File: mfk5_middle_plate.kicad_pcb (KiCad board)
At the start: 2 copper layers, 57.2 x 57.2 mm, 9 parts

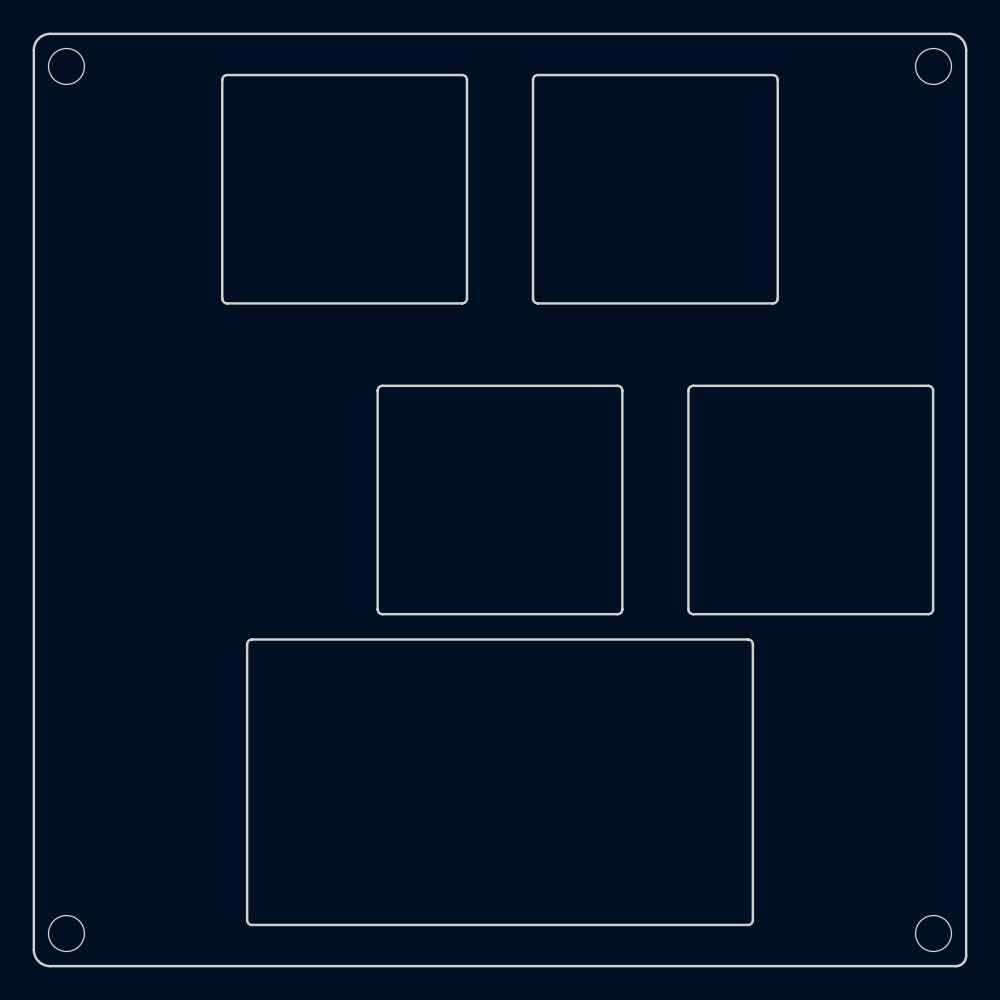
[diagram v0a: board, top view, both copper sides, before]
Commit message: Add ATmega32u4 and related components.
Stop using Pro Micro, going to use PCBA to SMT components.
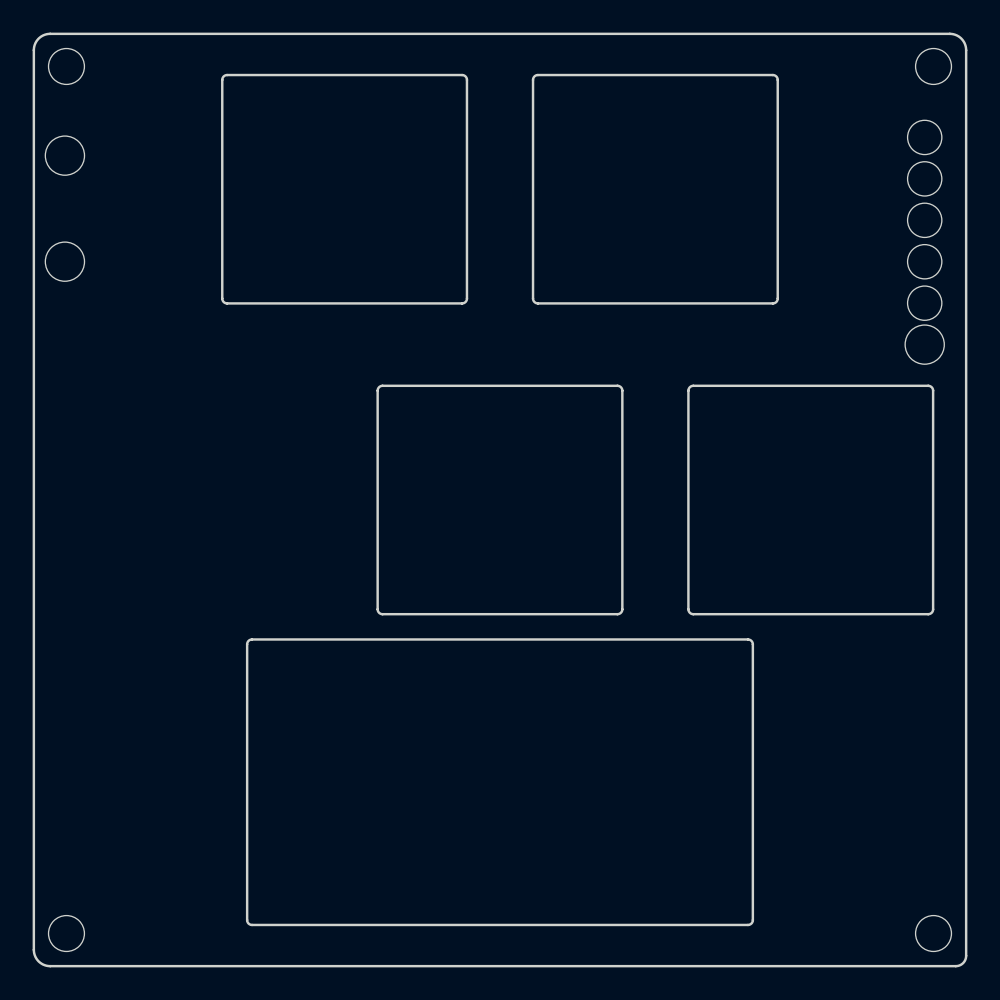
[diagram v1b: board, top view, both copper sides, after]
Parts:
- added REF**: , , F.Cu at (174.5, 95.0)
- added REF**: , , F.Cu at (174.5, 92.5)
- added REF**: , , F.Cu at (121.8, 90.0)
- added REF**: , , F.Cu at (122.5, 116.9)
- added REF**: , , F.Cu at (126.6, 125.6)
- added REF**: , , F.Cu at (170.8, 118.9)
- added REF**: , , F.Cu at (122.5, 125.6)
- added REF**: , , F.Cu at (174.5, 90.0)
- added REF**: , , F.Cu at (174.5, 87.4)
- added REF**: , , F.Cu at (166.8, 118.9)
- added REF**: , , F.Cu at (121.8, 83.5)
- added REF**: , , F.Cu at (165.6, 123.7)
- added REF**: , , F.Cu at (174.5, 82.3)
- added REF**: , , F.Cu at (173.8, 118.9)
- added REF**: , , F.Cu at (174.5, 84.9)
- added REF**: , , F.Cu at (126.6, 116.9)
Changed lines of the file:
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@@
   (title_block
     (title "mfk5 Middle Plate")
-    (date "2023-11-23")
-    (rev "2")
+    (date "2023-12-15")
+    (rev "3")
     (company "@niw")
   )
@@
   )
   (net 0 "")
+  (footprint "" (layer "F.Cu")
+    (at 174.46 95.05)
+    (fp_text reference "REF**" (at 0 0) (layer "F.SilkS") hide
+        (effects (font (size 1.27 1.27) (thickness 0.15)))
+    )
+    (fp_text value "" (at 0 0) (layer "F.SilkS") hide
+        (effects (font (size 1.27 1.27) (thickness 0.15)))
+    )
+    (pad "" np_thru_hole circle (at 0 0) (size 2.4 2.4) (drill 2.4) (layers "F&B.Cu" "*.Mask")
+      (pinfunction "Pin_1") (pintype "passive"))
+  )
+  (footprint "" (layer "F.Cu")
+    (at 121.755 83.465625)
+    (fp_text reference "REF**" (at 0 0) (layer "F.SilkS") hide
+        (effects (font (size 1.27 1.27) (thickness 0.15)))
+    )
+    (fp_text value "" (at 0 0) (layer "F.SilkS") hide
+        (effects (font (size 1.27 1.27) (thickness 0.15)))
+    )
+    (pad "" np_thru_hole circle (at 0 0 270) (size 2.4 2.4) (drill 2.4) (layers "F&B.Cu" "*.Mask")
+      (pinfunction "1") (pintype "passive"))
+  )
   (footprint "Gateron_Low_Profile:Gateron_Low_Profile_Middle_Plate" (layer "F.Cu")
     (at 157.95 85.525)
@@
     (pad "" np_thru_hole circle (at 0 0) (size 2.2 2.2) (drill 2.2) (layers "F&B.Cu" "*.Mask"))
   )
+  (footprint "" (layer "F.Cu")
+    (at 174.46 84.89)
+    (fp_text reference "REF**" (at 0 0) (layer "F.SilkS") hide
+        (effects (font (size 1.27 1.27) (thickness 0.15)))
+    )
+    (fp_text value "" (at 0 0) (layer "F.SilkS") hide
+        (effects (font (size 1.27 1.27) (thickness 0.15)))
+    )
+    (pad "" np_thru_hole circle (at 0 0) (size 2.1 2.1) (drill 2.1) (layers "F&B.Cu" "*.Mask")
+      (pinfunction "Pin_5") (pintype "passive"))
+  )
+  (footprint "" (layer "F.Cu")
+    (at 126.63 116.92375)
+    (fp_text reference "REF**" (at 0 0) (layer "F.SilkS") hide
+        (effects (font (size 1.27 1.27) (thickness 0.15)))
+    )
+    (fp_text value "" (at 0 0) (layer "F.SilkS") hide
+        (effects (font (size 1.27 1.27) (thickness 0.15)))
+    )
+    (pad "" np_thru_hole oval (at 0 0 90) (size 1.4 2.5) (drill oval 1.4 2.5) (layers "F&B.Cu" "*.Mask")
+      (pinfunction "SHIELD") (pintype "passive"))
+  )
+  (footprint "" (layer "F.Cu")
+    (at 174.46 92.51)
+    (fp_text reference "REF**" (at 0 0) (layer "F.SilkS") hide
+        (effects (font (size 1.27 1.27) (thickness 0.15)))
+    )
+    (fp_text value "" (at 0 0) (layer "F.SilkS") hide
+        (effects (font (size 1.27 1.27) (thickness 0.15)))
+    )
+    (pad "" np_thru_hole circle (at 0 0) (size 2.1 2.1) (drill 2.1) (layers "F&B.Cu" "*.Mask")
+      (pinfunction "Pin_2") (pintype "passive"))
+  )
+  (footprint "" (layer "F.Cu")
+    (at 121.755 89.965625)
+    (fp_text reference "REF**" (at 0 0) (layer "F.SilkS") hide
+        (effects (font (size 1.27 1.27) (thickness 0.15)))
+    )
+    (fp_text value "" (at 0 0) (layer "F.SilkS") hide
+        (effects (font (size 1.27 1.27) (thickness 0.15)))
+    )
+    (pad "" np_thru_hole circle (at 0 0 270) (size 2.4 2.4) (drill 2.4) (layers "F&B.Cu" "*.Mask")
+      (pinfunction "2") (pintype "passive"))
+  )
+  (footprint "" (layer "F.Cu")
+    (at 122.45 116.92375)
+    (fp_text reference "REF**" (at 0 0) (layer "F.SilkS") hide
+        (effects (font (size 1.27 1.27) (thickness 0.15)))
+    )
+    (fp_text value "" (at 0 0) (layer "F.SilkS") hide
+        (effects (font (size 1.27 1.27) (thickness 0.15)))
+    )
+    (pad "" np_thru_hole oval (at 0 0 90) (size 1.4 2) (drill oval 1.4 2) (layers "F&B.Cu" "*.Mask")
+      (pinfunction "SHIELD") (pintype "passive"))
+  )
+  (footprint "" (layer "F.Cu")
+    (at 126.63 125.56375)
+    (fp_text reference "REF**" (at 0 0) (layer "F.SilkS") hide
+        (effects (font (size 1.27 1.27) (thickness 0.15)))
+    )
+    (fp_text value "" (at 0 0) (layer "F.SilkS") hide
+        (effects (font (size 1.27 1.27) (thickness 0.15)))
+    )
+    (pad "" np_thru_hole oval (at 0 0 90) (size 1.4 2.5) (drill oval 1.4 2.5) (layers "F&B.Cu" "*.Mask")
+      (pinfunction "SHIELD") (pintype "passive"))
+  )
+  (footprint "" (layer "F.Cu")
+    (at 170.775 118.8625)
+    (fp_text reference "REF**" (at 0 0) (layer "F.SilkS") hide
+        (effects (font (size 1.27 1.27) (thickness 0.15)))
+    )
+    (fp_text value "" (at 0 0) (layer "F.SilkS") hide
+        (effects (font (size 1.27 1.27) (thickness 0.15)))
+    )
+    (pad "" np_thru_hole oval (at 0 0 90) (size 2 2.4) (drill oval 2 2.4) (layers "F&B.Cu" "*.Mask")
+      (pinfunction "Ring_1") (pintype "passive"))
+  )
+  (footprint "" (layer "F.Cu")
+    (at 122.45 125.56375)
+    (fp_text reference "REF**" (at 0 0) (layer "F.SilkS") hide
+        (effects (font (size 1.27 1.27) (thickness 0.15)))
+    )
+    (fp_text value "" (at 0 0) (layer "F.SilkS") hide
+        (effects (font (size 1.27 1.27) (thickness 0.15)))
+    )
+    (pad "" np_thru_hole oval (at 0 0 90) (size 1.4 2) (drill oval 1.4 2) (layers "F&B.Cu" "*.Mask")
+      (pinfunction "SHIELD") (pintype "passive"))
+  )
   (footprint "Gateron_Low_Profile:Gateron_Low_Profile_Middle_Plate_Stabilizer_2U" (layer "F.Cu")
     (at 148.425 123.625)
@@
     (fp_arc (start 15.5 6.7) (mid 15.412132 6.912132) (end 15.2 7)
       (stroke (width 0.15) (type default)) (layer "Edge.Cuts"))
+  )
+  (footprint "" (layer "F.Cu")
+    (at 174.46 89.97)
+    (fp_text reference "REF**" (at 0 0) (layer "F.SilkS") hide
+        (effects (font (size 1.27 1.27) (thickness 0.15)))
+    )
+    (fp_text value "" (at 0 0) (layer "F.SilkS") hide
+        (effects (font (size 1.27 1.27) (thickness 0.15)))
+    )
+    (pad "" np_thru_hole circle (at 0 0) (size 2.1 2.1) (drill 2.1) (layers "F&B.Cu" "*.Mask")
+      (pinfunction "Pin_3") (pintype "passive"))
+  )
+  (footprint "" (layer "F.Cu")
+    (at 174.46 87.43)
+    (fp_text reference "REF**" (at 0 0) (layer "F.SilkS") hide
+        (effects (font (size 1.27 1.27) (thickness 0.15)))
+    )
+    (fp_text value "" (at 0 0) (layer "F.SilkS") hide
+        (effects (font (size 1.27 1.27) (thickness 0.15)))
+    )
+    (pad "" np_thru_hole circle (at 0 0) (size 2.1 2.1) (drill 2.1) (layers "F&B.Cu" "*.Mask")
+      (pinfunction "Pin_4") (pintype "passive"))
+  )
+  (footprint "" (layer "F.Cu")
+    (at 166.775 118.8625)
+    (fp_text reference "REF**" (at 0 0) (layer "F.SilkS") hide
+        (effects (font (size 1.27 1.27) (thickness 0.15)))
+    )
+    (fp_text value "" (at 0 0) (layer "F.SilkS") hide
+        (effects (font (size 1.27 1.27) (thickness 0.15)))
+    )
+    (pad "" np_thru_hole oval (at 0 0 90) (size 2 2.4) (drill oval 2 2.4) (layers "F&B.Cu" "*.Mask")
+      (pinfunction "Tip") (pintype "passive"))
   )
   (footprint "MountingHole:MountingHole_2.2mm_M2" (layer "F.Cu")
@@
     (pad "" np_thru_hole circle (at 0 0) (size 2.2 2.2) (drill 2.2) (layers "F&B.Cu" "*.Mask"))
   )
+  (footprint "" (layer "F.Cu")
+    (at 165.575 123.6625)
+    (fp_text reference "REF**" (at 0 0) (layer "F.SilkS") hide
+        (effects (font (size 1.27 1.27) (thickness 0.15)))
+    )
+    (fp_text value "" (at 0 0) (layer "F.SilkS") hide
+        (effects (font (size 1.27 1.27) (thickness 0.15)))
+    )
+    (pad "" np_thru_hole oval (at 0 0 90) (size 2 2.4) (drill oval 2 2.4) (layers "F&B.Cu" "*.Mask")
+      (pinfunction "Sleeve") (pintype "passive"))
+  )
   (footprint "Gateron_Low_Profile:Gateron_Low_Profile_Middle_Plate" (layer "F.Cu")
     (at 138.9 85.525)
@@
       (stroke (width 0.15) (type default)) (layer "Edge.Cuts"))
   )
+  (footprint "" (layer "F.Cu")
+    (at 174.46 82.35)
+    (fp_text reference "REF**" (at 0 0) (layer "F.SilkS") hide
+        (effects (font (size 1.27 1.27) (thickness 0.15)))
+    )
+    (fp_text value "" (at 0 0) (layer "F.SilkS") hide
+        (effects (font (size 1.27 1.27) (thickness 0.15)))
+    )
+    (pad "" np_thru_hole circle (at 0 0) (size 2.1 2.1) (drill 2.1) (layers "F&B.Cu" "*.Mask")
+      (pinfunction "Pin_6") (pintype "passive"))
+  )
+  (footprint "" (layer "F.Cu")
+    (at 173.775 118.8625)
+    (fp_text reference "REF**" (at 0 0) (layer "F.SilkS") hide
+        (effects (font (size 1.27 1.27) (thickness 0.15)))
+    )
+    (fp_text value "" (at 0 0) (layer "F.SilkS") hide
+        (effects (font (size 1.27 1.27) (thickness 0.15)))
+    )
+    (pad "" np_thru_hole oval (at 0 0 90) (size 2 2.4) (drill oval 2 2.4) (layers "F&B.Cu" "*.Mask")
+      (pinfunction "Ring_2") (pintype "passive"))
+  )
   (footprint "MountingHole:MountingHole_2.2mm_M2" (layer "F.Cu")
